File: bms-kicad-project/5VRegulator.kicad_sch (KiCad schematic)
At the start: 44 parts, among them U5 SIC461ED-T1-GE3

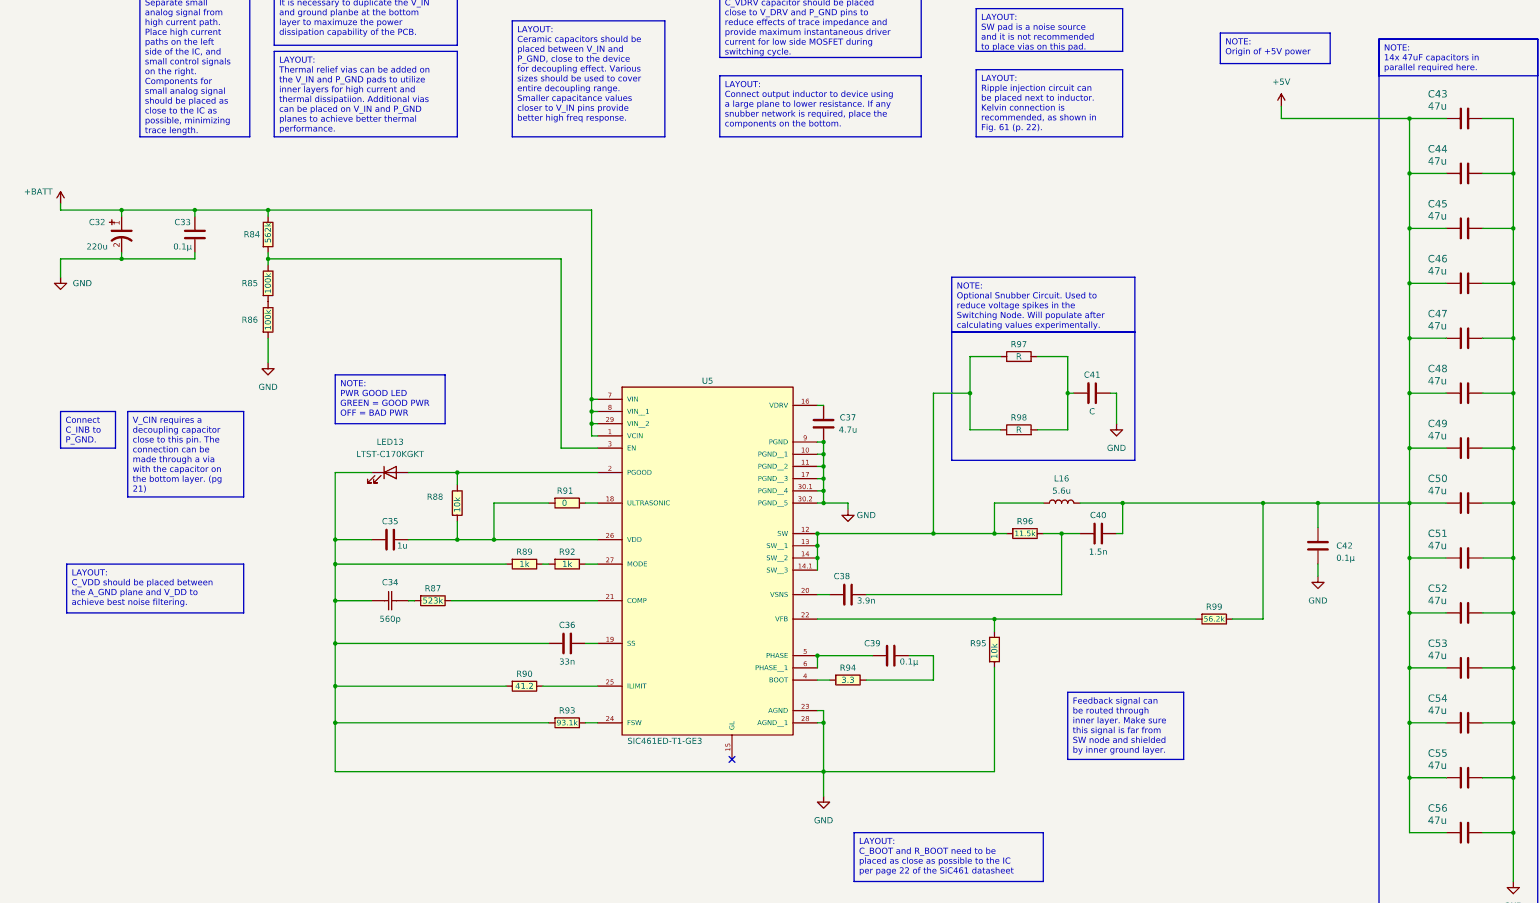
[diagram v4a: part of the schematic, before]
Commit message: Feature/current sensor (#17)
* feat: making sure my git still works

* feat: figured out battery stack monitor V+ biasing. Refer to task 5 on the punchlist for more details.

* feat: swapped out battery<->18V diode for cheaper alternative

* feat: started a new sheet for external connections and added current sensor

* feat: made a placeholder label to connect current sensor to LTC6811 GPIO

* feat: added remaining connectors to component library

* Wired up most external connections

* feat: Just shifting a few things around
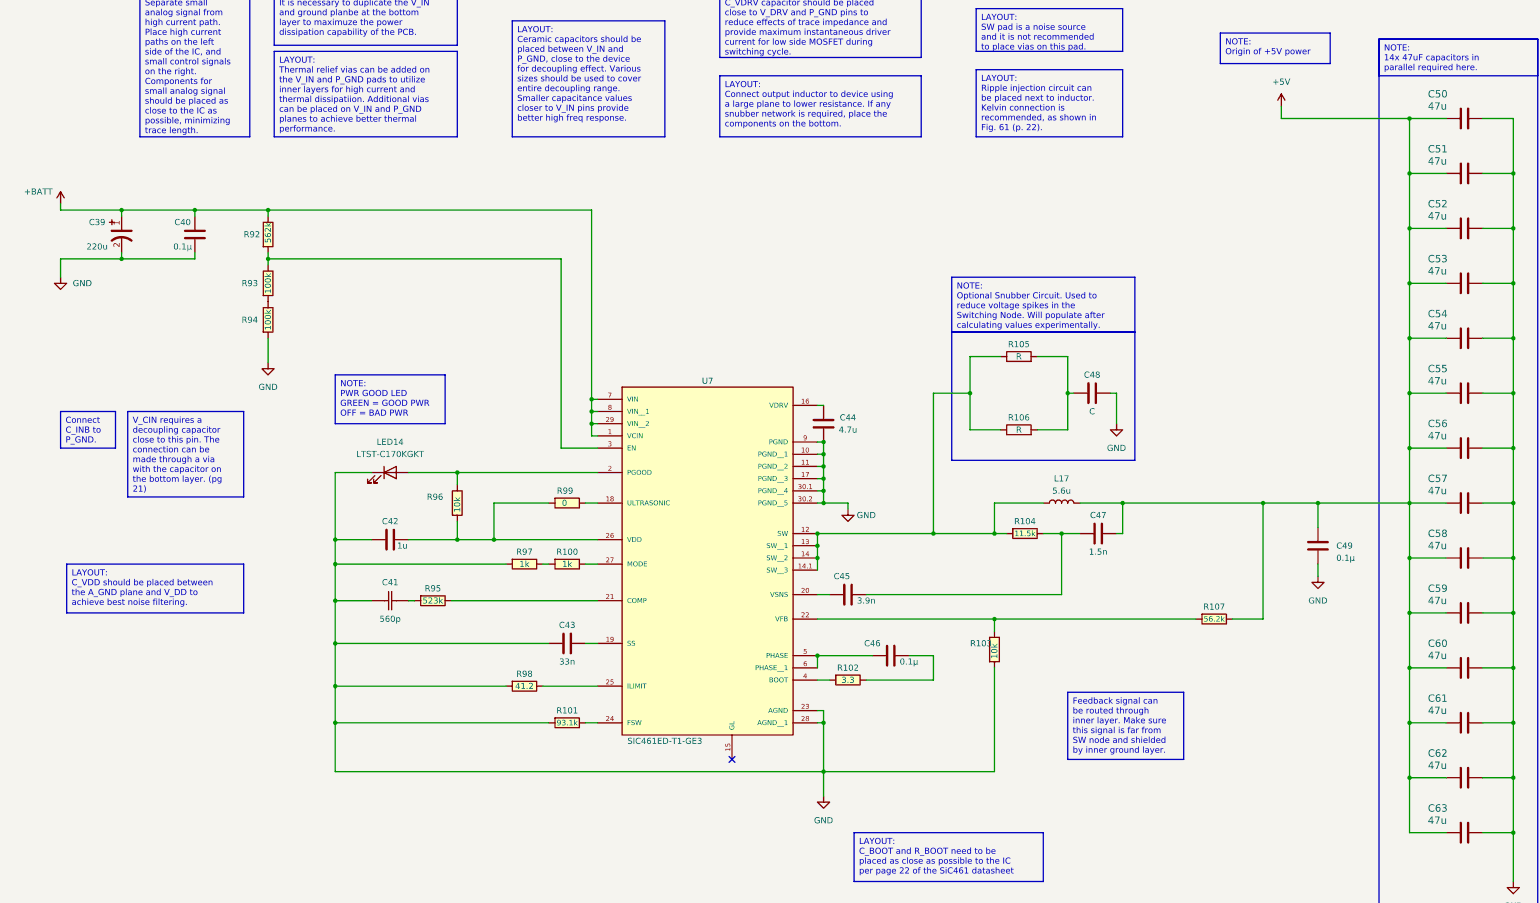
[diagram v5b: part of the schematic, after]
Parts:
- renumbered C32 to C39, C33 to C40, C34 to C41, C35 to C42, C36 to C43, C37 to C44, C38 to C45, C39 to C46, C40 to C47, C41 to C48, C42 to C49, C43 to C50, C44 to C51, C45 to C52, C46 to C53, C47 to C54, C48 to C55, C49 to C56, C50 to C57, C51 to C58, C52 to C59, C53 to C60, C54 to C61, C55 to C62, C56 to C63, L16 to L17, LED13 to LED14, R92 to R100, R93 to R101, R94 to R102, R95 to R103, R96 to R104, R97 to R105, R98 to R106, R99 to R107, R84 to R92, R85 to R93, R86 to R94, R87 to R95, R88 to R96, R89 to R97, R90 to R98, R91 to R99, U5 to U7

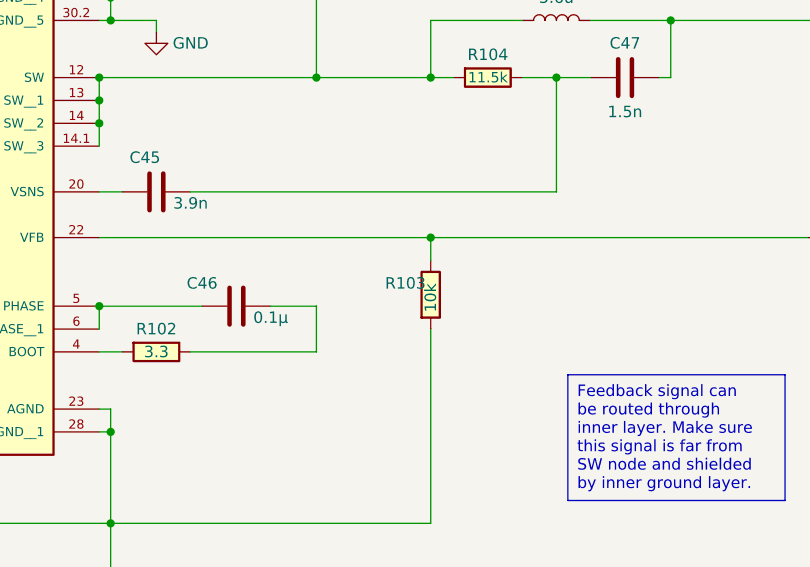
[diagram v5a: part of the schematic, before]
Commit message: feat: added sims directory, new cell balancing components
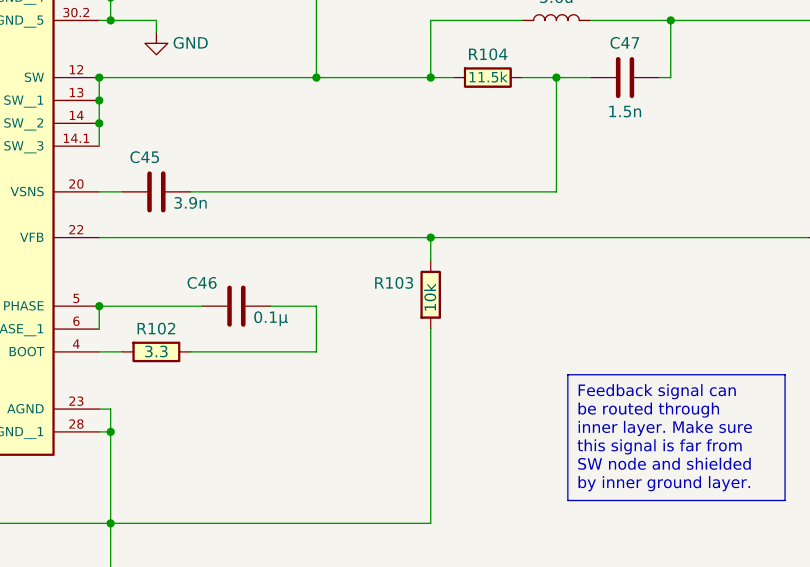
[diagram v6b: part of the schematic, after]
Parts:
- C40, C46, C49: Manufacturer Part Number (none) -> GCJ188R72A104KA01D
- R100, R97: Manufacturer Part Number (none) -> RC0805FR-071KL
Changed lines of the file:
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@@
+      (effects (font (size 1.27 1.27)) hide)
+    )
+    (property "Manufacturer Part Number" "GCJ188R72A104KA01D" (at 219.71 189.23 0)
       (effects (font (size 1.27 1.27)) hide)
     )
@@
       (effects (font (size 1.27 1.27)) hide)
     )
+    (property "Manufacturer Part Number" "RC0805FR-071KL" (at 135.89 147.32 0)
+      (effects (font (size 1.27 1.27)) hide)
+    )
     (pin "1")
     (pin "2")
@@
     )
     (property "Manufacturer_Part_Number" "GCJ188R72A104KA01D" (at 57.15 96.52 0)
+      (effects (font (size 1.27 1.27)) hide)
+    )
+    (property "Manufacturer Part Number" "GCJ188R72A104KA01D" (at 57.15 96.52 0)
       (effects (font (size 1.27 1.27)) hide)
     )
@@
       (effects (font (size 1.27 1.27)) hide)
     )
+    (property "Manufacturer Part Number" "GCJ188R72A104KA01D" (at 290.83 161.29 0)
+      (effects (font (size 1.27 1.27)) hide)
+    )
     (pin "2")
     (pin "1")
@@
       (effects (font (size 1.27 1.27)) hide)
     )
+    (property "Manufacturer Part Number" "RC0805FR-071KL" (at 144.78 147.32 0)
+      (effects (font (size 1.27 1.27)) hide)
+    )
     (pin "1")
     (pin "2")
@@
   (symbol (lib_id "FixedWing:RK73H2ATTD1002F") (at 234.95 180.34 90) (unit 1)
     (in_bom yes) (on_board yes) (dnp no)
-    (property "Reference" "R103" (at 229.87 175.26 90)
+    (property "Reference" "R103" (at 228.6 175.26 90)
       (effects (font (size 1.27 1.27)) (justify right))
     )

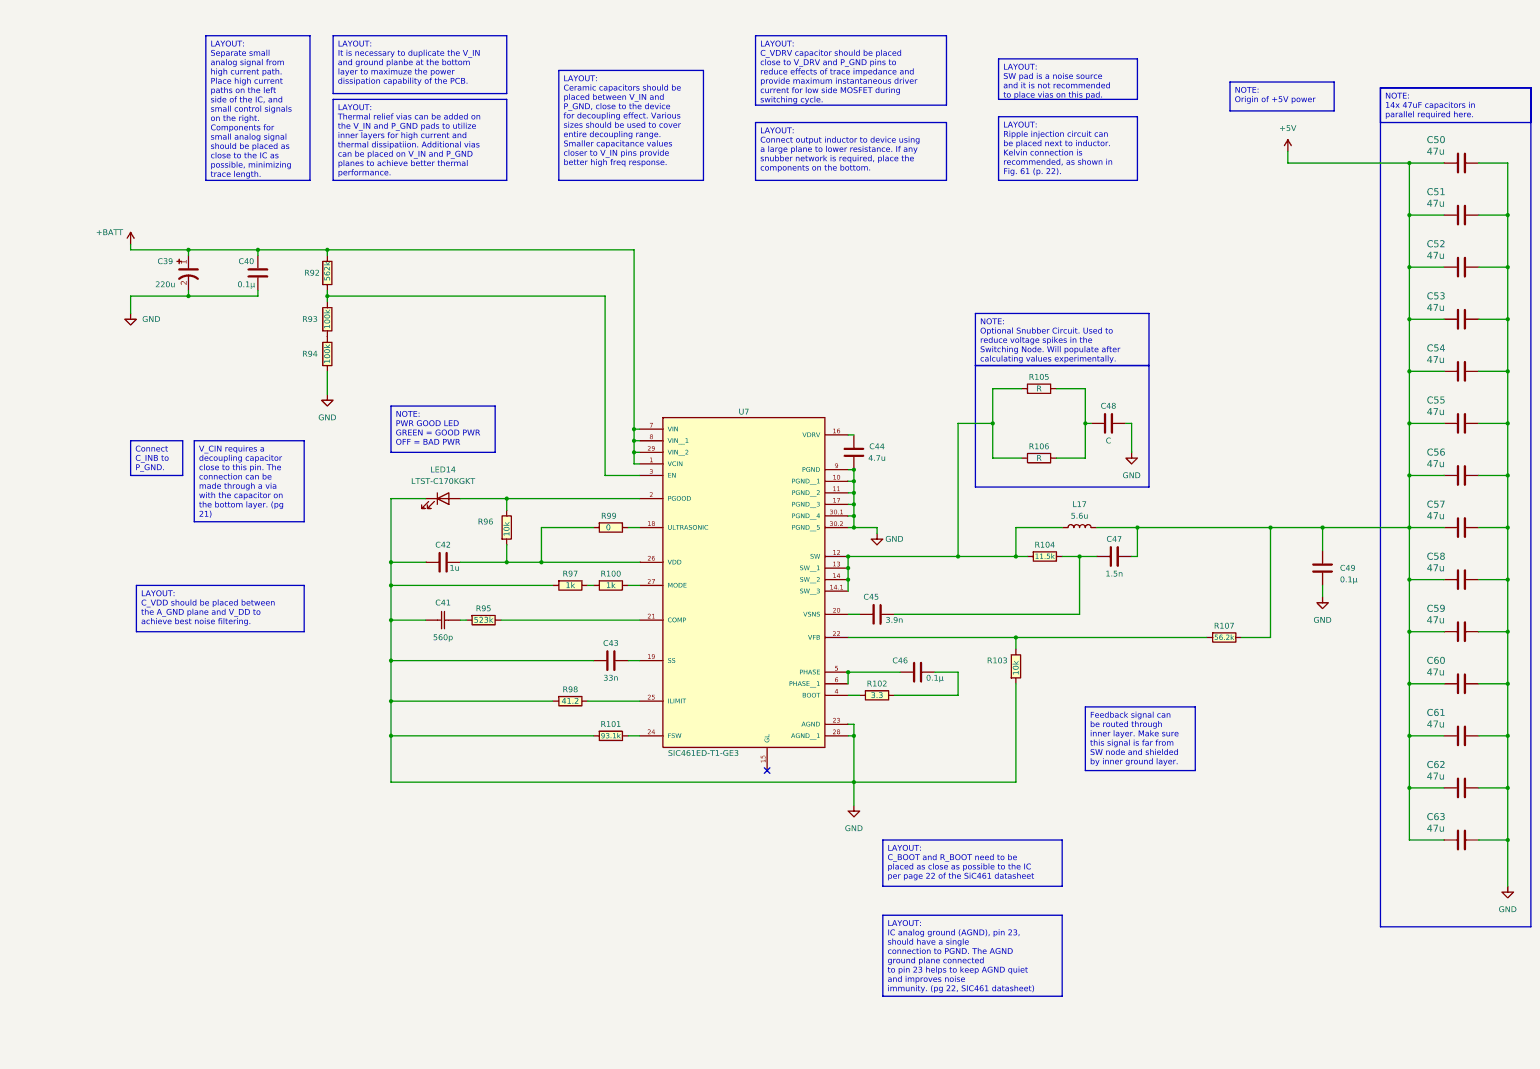
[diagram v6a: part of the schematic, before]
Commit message: feat: cell filtering/balancing switchover done
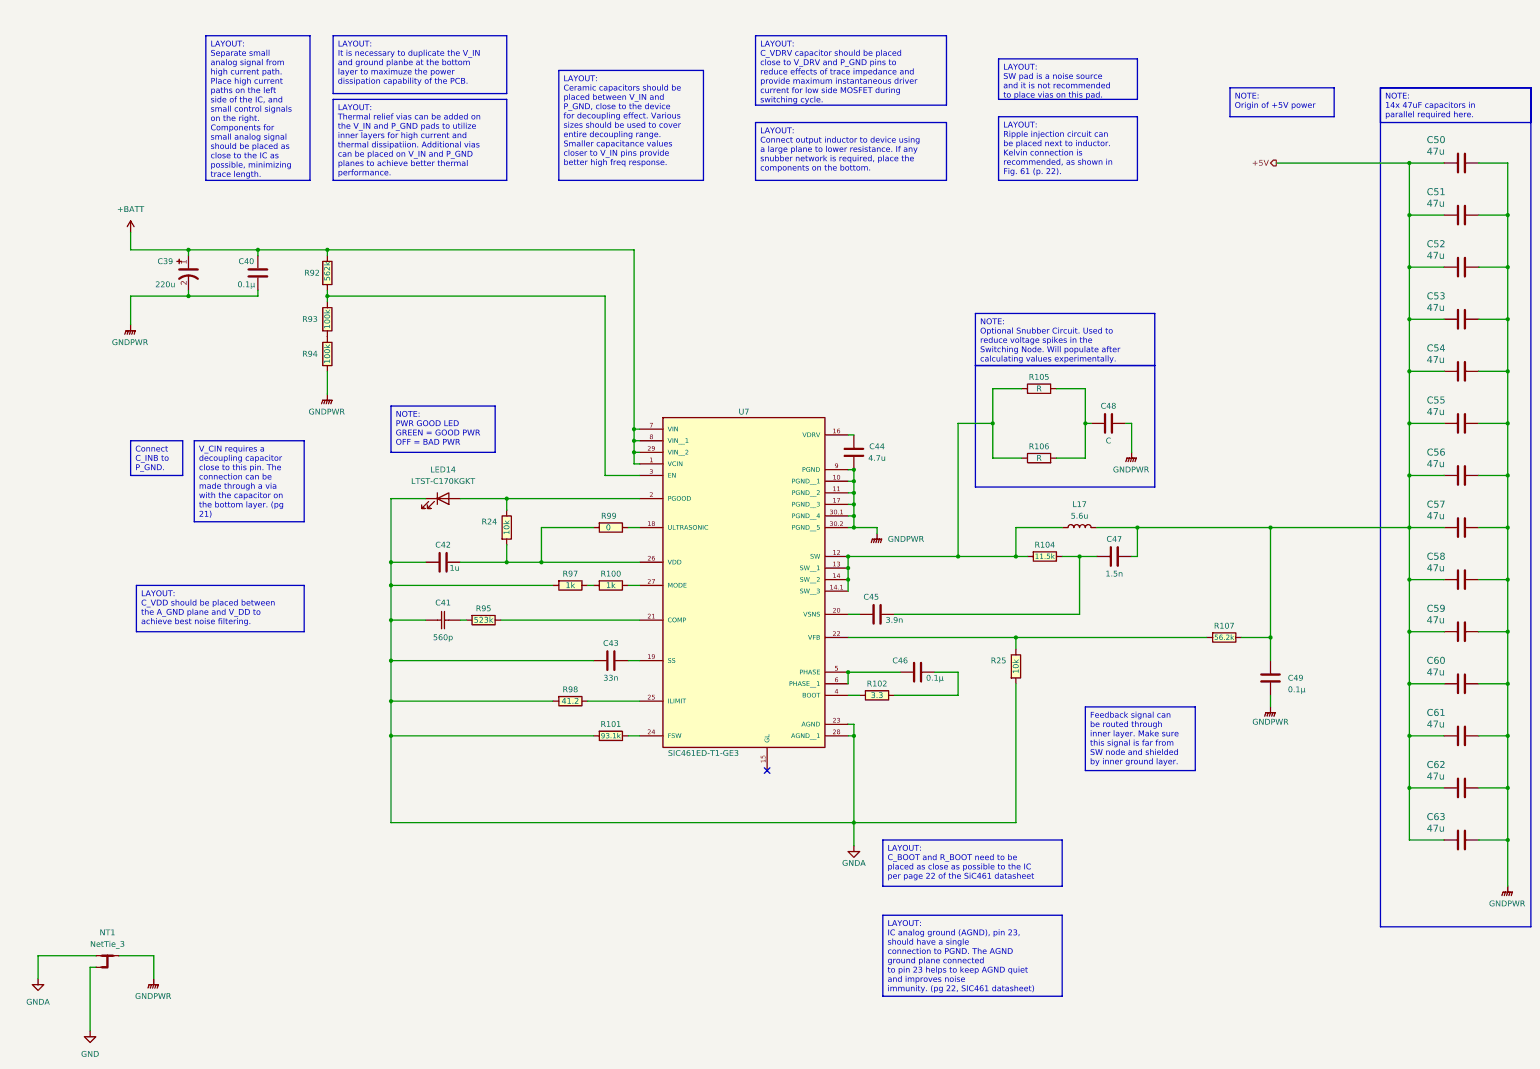
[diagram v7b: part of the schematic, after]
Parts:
- removed R103, R96: 10k, FixedWing:KOA_Speer-RK73H2A-0-0-MFG, symbol FixedWing:RK73H2ATTD1002F
- added NT1: NetTie_3, NetTie:NetTie-3_SMD_Pad2.0mm, symbol Device:NetTie_3
- added R24, R25: 10k, FixedWing:KOA_Speer-RK73H2A-0-0-MFG, symbol FixedWing:RK73H2ATTD1002F
- C39: symbol FixedWing:EEUFR1J221L -> FixedWing:80ZLH220MEFC10X23; Manufacturer Panasonic Electronic Components -> Rubycon; Manufacturer Part Number EEU-FR1J221L -> 80ZLH220MEFC10X23
- C40: Manufacturer_Part_Number GCJ188R72A104KA01D -> (none)
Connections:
- net GND: now also NT1.3; no longer C39.2 (N), C40.1, C41.1, C42.2, C43.1, C44.1, C48.2, C49.1, C50.1, C51.1, C52.1, C53.1, C54.1, C55.1, C56.1, C57.1, C58.1, C59.1, C60.1, C61.1, C62.1, C63.1, LED14.1 (K), R101.1, R94.1, R97.1, R98.1, U7.10 (PGND__1), U7.11 (PGND__2), U7.17 (PGND__3), U7.23 (AGND), U7.28 (AGND__1), U7.30.1 (PGND__4), U7.30.2 (PGND__5), U7.9 (PGND)
- net at LED14.2 (A), U7.2 (PGOOD): now also R24.2
- net at C42.1, R99.1, U7.26 (VDD): now also R24.1
- net at R107.1, U7.22 (VFB): now also R25.2
- new net GNDA: C41.1, C42.2, C43.1, LED14.1 (K), NT1.1, R101.1, R25.1, R97.1, R98.1, U7.23 (AGND), U7.28 (AGND__1)
- new net GNDPWR: C39.2 (N), C40.1, C44.1, C48.2, C49.1, C50.1, C51.1, C52.1, C53.1, C54.1, C55.1, C56.1, C57.1, C58.1, C59.1, C60.1, C61.1, C62.1, C63.1, NT1.2, R94.1, U7.10 (PGND__1), U7.11 (PGND__2), U7.17 (PGND__3), U7.30.1 (PGND__4), U7.30.2 (PGND__5), U7.9 (PGND)
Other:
- moved on the sheet: C49

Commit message: feat: don't even know what I changed, just zoned out for several hours. Made PCB r/a mount XT-60s and solder pads into a 2-for-1 deal
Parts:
- renumbered C39 to C40, C40 to C41, C41 to C42, C42 to C43, C43 to C44, C44 to C45, C45 to C46, C46 to C47, C47 to C48, C48 to C49, C49 to C50, C50 to C51, C51 to C52, C52 to C53, C53 to C54, C54 to C55, C55 to C56, C56 to C57, C57 to C58, C58 to C59, C59 to C60, C60 to C61, C61 to C62, C62 to C63, C63 to C64, L17 to L1, NT1 to NT2, R92 to R104, R93 to R105, R94 to R106, R95 to R107, R24 to R108, R97 to R109, R98 to R110, R99 to R111, R100 to R112, R101 to R113, R102 to R114, R25 to R115, R104 to R116, R105 to R117, R106 to R118, R107 to R119, U7 to U6
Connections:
- net GND: now also NT2.2; no longer NT2.3
- net GNDPWR: now also NT2.3; no longer NT2.2
